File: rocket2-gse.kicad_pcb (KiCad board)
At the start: 4 copper layers, 0 parts

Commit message: Add PCB basic functional blocks
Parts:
- added C1: 4.7uF, Capacitor_SMD:C_0603_1608Metric, F.Cu at (169.0, 137.0)
- added C10: 100nF, Capacitor_SMD:C_0402_1005Metric, F.Cu at (366.1, 71.8)
- added C11: 22uF, Capacitor_SMD:C_1206_3216Metric, F.Cu at (-127.0, 236.0)
- added C12: 100uF, Capacitor_SMD:C_1206_3216Metric, F.Cu at (-143.5, 236.0)
- added C13: 22uF, Capacitor_SMD:C_1206_3216Metric, F.Cu at (-92.5, 236.0)
- added C14: 100uF, Capacitor_SMD:C_1206_3216Metric, F.Cu at (-109.0, 236.0)
- added C15: 4.7uF, Capacitor_SMD:C_0603_1608Metric, F.Cu at (363.8, 78.5)
- added C16: 10uF, Capacitor_SMD:C_1206_3216Metric, F.Cu at (-127.0, 152.5)
- added C17: 10uF, Capacitor_SMD:C_1206_3216Metric, F.Cu at (-114.0, 152.5)
- added C18: 100nF, Capacitor_SMD:C_0402_1005Metric, F.Cu at (-136.0, 13.5)
- added C19: 100nF, Capacitor_SMD:C_0402_1005Metric, F.Cu at (-123.0, 13.6)
- added C2: 100nF, Capacitor_SMD:C_0402_1005Metric, F.Cu at (172.5, 137.0)
- added C20: 100nF, Capacitor_SMD:C_0402_1005Metric, F.Cu at (-110.0, 13.5)
- added C21: 100nF, Capacitor_SMD:C_0402_1005Metric, F.Cu at (-97.0, 13.5)
- added C22: 100nF, Capacitor_SMD:C_0402_1005Metric, F.Cu at (-84.0, 13.5)
- added C23: 100nF, Capacitor_SMD:C_0402_1005Metric, F.Cu at (-71.0, 13.5)
- added C24: 100nF, Capacitor_SMD:C_0402_1005Metric, F.Cu at (-58.0, 13.5)
- added C25: 100nF, Capacitor_SMD:C_0402_1005Metric, F.Cu at (-45.0, 13.5)
- added C26: 100nF, Capacitor_SMD:C_0402_1005Metric, F.Cu at (-32.0, 13.5)
- added C27: 100nF, Capacitor_SMD:C_0402_1005Metric, F.Cu at (-136.5, 62.5)
- added C28: 100nF, Capacitor_SMD:C_0402_1005Metric, F.Cu at (-123.5, 62.5)
- added C29: 100nF, Capacitor_SMD:C_0402_1005Metric, F.Cu at (-110.5, 62.5)
- added C3: 100nF, Capacitor_SMD:C_0402_1005Metric, F.Cu at (176.0, 150.5)
- added C30: 100nF, Capacitor_SMD:C_0402_1005Metric, F.Cu at (-97.5, 62.5)
- added C31: 100nF, Capacitor_SMD:C_0402_1005Metric, F.Cu at (-84.5, 62.5)
- added C32: 100nF, Capacitor_SMD:C_0402_1005Metric, F.Cu at (-137.0, 105.5)
- added C33: 10nF, Capacitor_SMD:C_0402_1005Metric, F.Cu at (-141.0, 108.0)
- added C34: 10nF, Capacitor_SMD:C_0402_1005Metric, F.Cu at (-121.0, 108.0)
- added C35: 100nF, Capacitor_SMD:C_0402_1005Metric, F.Cu at (-117.0, 105.5)
- added C36: 10nF, Capacitor_SMD:C_0402_1005Metric, F.Cu at (-101.0, 108.0)
- added C37: 100nF, Capacitor_SMD:C_0402_1005Metric, F.Cu at (-97.0, 105.5)
- added C38: 10nF, Capacitor_SMD:C_0402_1005Metric, F.Cu at (-81.0, 108.0)
- added C39: 100nF, Capacitor_SMD:C_0402_1005Metric, F.Cu at (-77.0, 105.5)
- added C4: 100nF, Capacitor_SMD:C_0402_1005Metric, F.Cu at (182.5, 150.5)
- added C40: 10nF, Capacitor_SMD:C_0402_1005Metric, F.Cu at (-61.0, 108.0)
- added C41: 100nF, Capacitor_SMD:C_0402_1005Metric, F.Cu at (-57.0, 105.5)
- added C42: 10nF, Capacitor_SMD:C_0402_1005Metric, F.Cu at (-41.0, 108.0)
- added C43: 100nF, Capacitor_SMD:C_0402_1005Metric, F.Cu at (-37.0, 105.5)
- added C44: 100nF, Capacitor_SMD:C_0402_1005Metric, F.Cu at (169.0, 139.0)
- added C5: 100nF, Capacitor_SMD:C_0402_1005Metric, F.Cu at (186.0, 137.0)
- added C6: 100nF, Capacitor_SMD:C_0402_1005Metric, F.Cu at (175.5, 133.5)
- added C7: 1uF, Capacitor_SMD:C_0402_1005Metric, F.Cu at (168.5, 144.0)
- added C8: 100nF, Capacitor_SMD:C_0402_1005Metric, F.Cu at (169.5, 144.0)
- added C9: 10nF, Capacitor_SMD:C_0402_1005Metric, F.Cu at (170.5, 144.0)
- added D1: SDT8A100P5-7, Diode_SMD:D_PowerDI-5, F.Cu at (-139.0, 187.6)
- added D10: SDT8A100P5-7, Diode_SMD:D_PowerDI-5, F.Cu at (-141.0, 26.0)
- added D11: MMSZ4684T1G, Diode_SMD:D_SOD-123, F.Cu at (-142.0, 17.0)
- added D12: SDT8A100P5-7, Diode_SMD:D_PowerDI-5, F.Cu at (-128.0, 26.1)
- added D13: MMSZ4684T1G, Diode_SMD:D_SOD-123, F.Cu at (-129.0, 17.1)
- added D14: SDT8A100P5-7, Diode_SMD:D_PowerDI-5, F.Cu at (-115.0, 26.0)
- added D15: MMSZ4684T1G, Diode_SMD:D_SOD-123, F.Cu at (-116.0, 17.0)
- added D16: SDT8A100P5-7, Diode_SMD:D_PowerDI-5, F.Cu at (-102.0, 26.0)
- added D17: MMSZ4684T1G, Diode_SMD:D_SOD-123, F.Cu at (-103.0, 17.0)
- added D18: SDT8A100P5-7, Diode_SMD:D_PowerDI-5, F.Cu at (-89.0, 26.0)
- added D19: MMSZ4684T1G, Diode_SMD:D_SOD-123, F.Cu at (-90.0, 17.0)
- added D2: SDT8A100P5-7, Diode_SMD:D_PowerDI-5, F.Cu at (-119.0, 187.6)
- added D20: SDT8A100P5-7, Diode_SMD:D_PowerDI-5, F.Cu at (-76.0, 26.0)
- added D21: MMSZ4684T1G, Diode_SMD:D_SOD-123, F.Cu at (-77.0, 17.0)
- added D22: SDT8A100P5-7, Diode_SMD:D_PowerDI-5, F.Cu at (-63.0, 26.0)
- added D23: MMSZ4684T1G, Diode_SMD:D_SOD-123, F.Cu at (-64.0, 17.0)
- added D24: SDT8A100P5-7, Diode_SMD:D_PowerDI-5, F.Cu at (-50.0, 26.0)
- added D25: MMSZ4684T1G, Diode_SMD:D_SOD-123, F.Cu at (-51.0, 17.0)
- added D26: SDT8A100P5-7, Diode_SMD:D_PowerDI-5, F.Cu at (-37.0, 26.0)
- added D27: MMSZ4684T1G, Diode_SMD:D_SOD-123, F.Cu at (-38.0, 17.0)
- added D28: BZV55-B5V1, Diode_SMD:D_MiniMELF, F.Cu at (-140.0, 68.0)
- added D29: BZV55-B5V1, Diode_SMD:D_MiniMELF, F.Cu at (-127.0, 68.0)
- added D3: SDT8A100P5-7, Diode_SMD:D_PowerDI-5, F.Cu at (-129.4, 230.5)
- added D30: BZV55-B5V1, Diode_SMD:D_MiniMELF, F.Cu at (-114.0, 68.0)
- added D31: BZV55-B5V1, Diode_SMD:D_MiniMELF, F.Cu at (-101.0, 68.0)
- added D32: BZV55-B5V1, Diode_SMD:D_MiniMELF, F.Cu at (-88.0, 68.0)
- added D4: SDT8A100P5-7, Diode_SMD:D_PowerDI-5, F.Cu at (-94.9, 230.5)
- added D5: LED, LED_SMD:LED_0603_1608Metric, F.Cu at (-145.0, 188.5)
- added D6: LED, LED_SMD:LED_0603_1608Metric, F.Cu at (-125.0, 188.5)
- added D7: LED, LED_SMD:LED_0603_1608Metric, F.Cu at (338.4, 69.4)
- added D8: LED, LED_SMD:LED_0603_1608Metric, F.Cu at (-150.5, 238.0)
- added D9: LED, LED_SMD:LED_0603_1608Metric, F.Cu at (-116.0, 238.0)
- added F1: ~, Fuse:Fuseholder_Blade_Mini_Keystone_3568, F.Cu at (333.3, 54.0)
- added FB1: BLM18PG471SH1D, Inductor_SMD:L_0603_1608Metric, F.Cu at (-137.0, 109.0)
- added FB10: BLM18PG471SH1D, Inductor_SMD:L_0603_1608Metric, F.Cu at (-65.0, 109.0)
- added FB11: BLM18PG471SH1D, Inductor_SMD:L_0603_1608Metric, F.Cu at (-37.0, 109.0)
- added FB12: BLM18PG471SH1D, Inductor_SMD:L_0603_1608Metric, F.Cu at (-45.0, 109.0)
- added FB2: BLM18PG471SH1D, Inductor_SMD:L_0603_1608Metric, F.Cu at (-145.0, 109.0)
- added FB3: BLM18PG471SH1D, Inductor_SMD:L_0603_1608Metric, F.Cu at (-117.0, 109.0)
- added FB4: BLM18PG471SH1D, Inductor_SMD:L_0603_1608Metric, F.Cu at (-125.0, 109.0)
- added FB5: BLM18PG471SH1D, Inductor_SMD:L_0603_1608Metric, F.Cu at (-97.0, 109.0)
- added FB6: BLM18PG471SH1D, Inductor_SMD:L_0603_1608Metric, F.Cu at (-105.0, 109.0)
- added FB7: BLM18PG471SH1D, Inductor_SMD:L_0603_1608Metric, F.Cu at (-77.0, 109.0)
- added FB8: BLM18PG471SH1D, Inductor_SMD:L_0603_1608Metric, F.Cu at (-85.0, 109.0)
- added FB9: BLM18PG471SH1D, Inductor_SMD:L_0603_1608Metric, F.Cu at (-57.0, 109.0)
- added J1: ARM Cortex Debug, Connector_PinHeader_1.27mm:PinHeader_2x05_P1.27mm_Vertical_SMD, F.Cu at (191.0, 133.0)
- added J10: Solenoid, TerminalBlock:TerminalBlock_bornier-3_P5.08mm, F.Cu at (-128.0, 33.0)
- added J11: Solenoid, TerminalBlock:TerminalBlock_bornier-3_P5.08mm, F.Cu at (-115.0, 32.9)
- added J12: Solenoid, TerminalBlock:TerminalBlock_bornier-3_P5.08mm, F.Cu at (-102.0, 32.9)
- added J13: Solenoid, TerminalBlock:TerminalBlock_bornier-3_P5.08mm, F.Cu at (-89.0, 32.9)
- added J14: Solenoid, TerminalBlock:TerminalBlock_bornier-3_P5.08mm, F.Cu at (-76.0, 32.9)
- added J15: Solenoid, TerminalBlock:TerminalBlock_bornier-3_P5.08mm, F.Cu at (-63.0, 32.9)
- added J16: Solenoid, TerminalBlock:TerminalBlock_bornier-3_P5.08mm, F.Cu at (-50.0, 32.9)
- added J17: Solenoid, TerminalBlock:TerminalBlock_bornier-3_P5.08mm, F.Cu at (-37.0, 32.9)
- added J18: PT, TerminalBlock:TerminalBlock_bornier-3_P5.08mm, F.Cu at (-141.0, 75.9)
- added J19: PT, TerminalBlock:TerminalBlock_bornier-3_P5.08mm, F.Cu at (-128.0, 75.9)
- added J2: PWR0, Connector_BarrelJack:BarrelJack_Horizontal, F.Cu at (-141.0, 194.0)
- added J20: PT, TerminalBlock:TerminalBlock_bornier-3_P5.08mm, F.Cu at (-115.0, 75.9)
- added J21: PT, TerminalBlock:TerminalBlock_bornier-3_P5.08mm, F.Cu at (-102.0, 75.9)
- added J22: PT, TerminalBlock:TerminalBlock_bornier-3_P5.08mm, F.Cu at (-89.0, 75.9)
- added J3: PWR1, Connector_BarrelJack:BarrelJack_Horizontal, F.Cu at (-121.0, 194.0)
- added J4: USB-C, Connector_USB:USB_C_Receptacle_GCT_USB4105-xx-A_16P_TopMnt_Horizontal, F.Cu at (350.1, 32.2)
- added J5: ALARM, TerminalBlock:TerminalBlock_bornier-2_P5.08mm, F.Cu at (345.1, 42.2)
- added J6: ARM, TerminalBlock:TerminalBlock_bornier-2_P5.08mm, F.Cu at (-141.0, 159.9)
- added J7: E-MATCH, TerminalBlock:TerminalBlock_bornier-2_P5.08mm, F.Cu at (-125.0, 159.9)
- added J8: E-MATCH, TerminalBlock:TerminalBlock_bornier-2_P5.08mm, F.Cu at (-112.0, 159.9)
- added J9: Solenoid, TerminalBlock:TerminalBlock_bornier-3_P5.08mm, F.Cu at (-141.0, 32.9)
- added L1: SRR1208-220ML, Inductor_SMD:L_Bourns_SRR1208_12.7x12.7mm, F.Cu at (-141.0, 228.0)
- added L2: SRR1208-220ML, Inductor_SMD:L_Bourns_SRR1208_12.7x12.7mm, F.Cu at (-106.5, 228.0)
- added Q1: DMP3099L, Package_TO_SOT_SMD:SOT-23-3, F.Cu at (-131.5, 235.0)
- added Q10: DMG3402L, Package_TO_SOT_SMD:SOT-23-3, F.Cu at (-109.0, 26.0)
- added Q11: DMG3402L, Package_TO_SOT_SMD:SOT-23-3, F.Cu at (-96.0, 26.0)
- added Q12: DMG3402L, Package_TO_SOT_SMD:SOT-23-3, F.Cu at (-83.0, 26.0)
- added Q13: DMG3402L, Package_TO_SOT_SMD:SOT-23-3, F.Cu at (-70.0, 26.0)
- added Q14: DMG3402L, Package_TO_SOT_SMD:SOT-23-3, F.Cu at (-57.0, 26.0)
- added Q15: DMG3402L, Package_TO_SOT_SMD:SOT-23-3, F.Cu at (-44.0, 26.0)
- added Q16: DMG3402L, Package_TO_SOT_SMD:SOT-23-3, F.Cu at (-31.0, 26.0)
- added Q2: DMP3099L, Package_TO_SOT_SMD:SOT-23-3, F.Cu at (-97.0, 235.0)
- added Q3: DMG3402L, Package_TO_SOT_SMD:SOT-23-3, F.Cu at (359.2, 76.0)
- added Q4: DMG3402L, Package_TO_SOT_SMD:SOT-23-3, F.Cu at (-123.0, 152.5)
- added Q5: DMG3402L, Package_TO_SOT_SMD:SOT-23-3, F.Cu at (-118.5, 151.5)
- added Q6: DMG3402L, Package_TO_SOT_SMD:SOT-23-3, F.Cu at (-110.0, 152.5)
- added Q7: DMG3402L, Package_TO_SOT_SMD:SOT-23-3, F.Cu at (-105.5, 151.5)
- added Q8: DMG3402L, Package_TO_SOT_SMD:SOT-23-3, F.Cu at (-135.0, 26.0)
- added Q9: DMG3402L, Package_TO_SOT_SMD:SOT-23-3, F.Cu at (-122.0, 26.1)
- added R1: 10K, Resistor_SMD:R_0402_1005Metric, F.Cu at (357.4, 27.9)
- added R10: 3.3K, Resistor_SMD:R_0402_1005Metric, F.Cu at (-142.5, 188.5)
- added R11: 3.3K, Resistor_SMD:R_0402_1005Metric, F.Cu at (-122.5, 188.5)
- added R12: 3.3K, Resistor_SMD:R_0402_1005Metric, F.Cu at (363.2, 29.9)
- added R13: 1K, Resistor_SMD:R_0402_1005Metric, F.Cu at (-148.0, 238.0)
- added R14: 470R, Resistor_SMD:R_0402_1005Metric, F.Cu at (-113.5, 238.0)
- added R15: 5.1K, Resistor_SMD:R_0402_1005Metric, F.Cu at (363.2, 35.9)
- added R16: 5.1K, Resistor_SMD:R_0402_1005Metric, F.Cu at (366.1, 27.9)
- added R17: 10K, Resistor_SMD:R_0402_1005Metric, F.Cu at (366.1, 29.9)
- added R18: 100R, Resistor_SMD:R_0402_1005Metric, F.Cu at (366.1, 31.9)
- added R19: 100K, Resistor_SMD:R_0402_1005Metric, F.Cu at (-138.5, 154.0)
- added R2: 100K, Resistor_SMD:R_0402_1005Metric, F.Cu at (-142.5, 190.5)
- added R20: 15K, Resistor_SMD:R_0402_1005Metric, F.Cu at (-138.5, 151.5)
- added R21: 10K, Resistor_SMD:R_0402_1005Metric, F.Cu at (-124.0, 148.5)
- added R22: 100R, Resistor_SMD:R_0402_1005Metric, F.Cu at (-122.0, 149.0)
- added R23: 33K, Resistor_SMD:R_0402_1005Metric, F.Cu at (-120.0, 154.5)
- added R24: 10K, Resistor_SMD:R_0402_1005Metric, F.Cu at (-118.0, 154.5)
- added R25: 10K, Resistor_SMD:R_0402_1005Metric, F.Cu at (-119.0, 148.5)
- added R26: 10K, Resistor_SMD:R_0402_1005Metric, F.Cu at (-111.0, 148.5)
- added R27: 100R, Resistor_SMD:R_0402_1005Metric, F.Cu at (-109.0, 149.0)
- added R28: 33K, Resistor_SMD:R_0402_1005Metric, F.Cu at (-107.0, 154.5)
- added R29: 10K, Resistor_SMD:R_0402_1005Metric, F.Cu at (-105.0, 154.5)
- added R3: 15K, Resistor_SMD:R_0402_1005Metric, F.Cu at (-144.5, 190.5)
- added R30: 10K, Resistor_SMD:R_0402_1005Metric, F.Cu at (-106.0, 148.5)
- added R31: 10K, Resistor_SMD:R_0402_1005Metric, F.Cu at (-134.0, 19.5)
- added R32: 100R, Resistor_SMD:R_0402_1005Metric, F.Cu at (-134.0, 22.5)
- added R33: 1R, Resistor_SMD:R_2512_6332Metric, F.Cu at (-141.0, 21.0)
- added R34: 1K, Resistor_SMD:R_0402_1005Metric, F.Cu at (-136.5, 19.0)
- added R35: 10K, Resistor_SMD:R_0402_1005Metric, F.Cu at (-121.0, 19.6)
- added R36: 100R, Resistor_SMD:R_0402_1005Metric, F.Cu at (-121.0, 22.6)
- added R37: 1R, Resistor_SMD:R_2512_6332Metric, F.Cu at (-128.0, 21.1)
- added R38: 1K, Resistor_SMD:R_0402_1005Metric, F.Cu at (-123.5, 19.1)
- added R39: 10K, Resistor_SMD:R_0402_1005Metric, F.Cu at (-108.0, 19.5)
- added R4: 100K, Resistor_SMD:R_0402_1005Metric, F.Cu at (-122.5, 190.5)
- added R40: 100R, Resistor_SMD:R_0402_1005Metric, F.Cu at (-108.0, 22.5)
- added R41: 1R, Resistor_SMD:R_2512_6332Metric, F.Cu at (-115.0, 21.0)
- added R42: 1K, Resistor_SMD:R_0402_1005Metric, F.Cu at (-110.5, 19.0)
- added R43: 10K, Resistor_SMD:R_0402_1005Metric, F.Cu at (-95.0, 19.5)
- added R44: 100R, Resistor_SMD:R_0402_1005Metric, F.Cu at (-95.0, 22.5)
- added R45: 1R, Resistor_SMD:R_2512_6332Metric, F.Cu at (-102.0, 21.0)
- added R46: 1K, Resistor_SMD:R_0402_1005Metric, F.Cu at (-97.5, 19.0)
- added R47: 10K, Resistor_SMD:R_0402_1005Metric, F.Cu at (-82.0, 19.5)
- added R48: 100R, Resistor_SMD:R_0402_1005Metric, F.Cu at (-82.0, 22.5)
- added R49: 1R, Resistor_SMD:R_2512_6332Metric, F.Cu at (-89.0, 21.0)
- added R5: 15K, Resistor_SMD:R_0402_1005Metric, F.Cu at (-124.5, 190.5)
- added R50: 1K, Resistor_SMD:R_0402_1005Metric, F.Cu at (-84.5, 19.0)
- added R51: 10K, Resistor_SMD:R_0402_1005Metric, F.Cu at (-69.0, 19.5)
- added R52: 100R, Resistor_SMD:R_0402_1005Metric, F.Cu at (-69.0, 22.5)
- added R53: 1R, Resistor_SMD:R_2512_6332Metric, F.Cu at (-76.0, 21.0)
- added R54: 1K, Resistor_SMD:R_0402_1005Metric, F.Cu at (-71.5, 19.0)
- added R55: 10K, Resistor_SMD:R_0402_1005Metric, F.Cu at (-56.0, 19.5)
- added R56: 100R, Resistor_SMD:R_0402_1005Metric, F.Cu at (-56.0, 22.5)
- added R57: 1R, Resistor_SMD:R_2512_6332Metric, F.Cu at (-63.0, 21.0)
- added R58: 1K, Resistor_SMD:R_0402_1005Metric, F.Cu at (-58.5, 19.0)
- added R59: 10K, Resistor_SMD:R_0402_1005Metric, F.Cu at (-43.0, 19.5)
- added R6: 100K, Resistor_SMD:R_0402_1005Metric, F.Cu at (-144.0, 238.0)
- added R60: 100R, Resistor_SMD:R_0402_1005Metric, F.Cu at (-43.0, 22.5)
- added R61: 1R, Resistor_SMD:R_2512_6332Metric, F.Cu at (-50.0, 21.0)
- added R62: 1K, Resistor_SMD:R_0402_1005Metric, F.Cu at (-45.5, 19.0)
- added R63: 10K, Resistor_SMD:R_0402_1005Metric, F.Cu at (-30.0, 19.5)
- added R64: 100R, Resistor_SMD:R_0402_1005Metric, F.Cu at (-30.0, 22.5)
- added R65: 1R, Resistor_SMD:R_2512_6332Metric, F.Cu at (-37.0, 21.0)
- added R66: 1K, Resistor_SMD:R_0402_1005Metric, F.Cu at (-32.5, 19.0)
- added R67: 1K, Resistor_SMD:R_0402_1005Metric, F.Cu at (-138.0, 70.5)
- added R68: 5K, Resistor_SMD:R_0402_1005Metric, F.Cu at (-135.5, 68.0)
- added R69: 10K, Resistor_SMD:R_0402_1005Metric, F.Cu at (-135.5, 70.5)
- added R7: 33K, Resistor_SMD:R_0402_1005Metric, F.Cu at (-142.0, 238.0)
- added R70: 1K, Resistor_SMD:R_0402_1005Metric, F.Cu at (-125.0, 70.5)
- added R71: 5K, Resistor_SMD:R_0402_1005Metric, F.Cu at (-122.5, 68.0)
- added R72: 10K, Resistor_SMD:R_0402_1005Metric, F.Cu at (-122.5, 70.5)
- added R73: 1K, Resistor_SMD:R_0402_1005Metric, F.Cu at (-112.0, 70.5)
- added R74: 5K, Resistor_SMD:R_0402_1005Metric, F.Cu at (-109.5, 68.0)
- added R75: 10K, Resistor_SMD:R_0402_1005Metric, F.Cu at (-109.5, 70.5)
- added R76: 1K, Resistor_SMD:R_0402_1005Metric, F.Cu at (-99.0, 70.5)
- added R77: 5K, Resistor_SMD:R_0402_1005Metric, F.Cu at (-96.5, 68.0)
- added R78: 10K, Resistor_SMD:R_0402_1005Metric, F.Cu at (-96.5, 70.5)
- added R79: 1K, Resistor_SMD:R_0402_1005Metric, F.Cu at (-86.0, 70.5)
- added R8: 33K, Resistor_SMD:R_0402_1005Metric, F.Cu at (-109.5, 238.0)
- added R80: 5K, Resistor_SMD:R_0402_1005Metric, F.Cu at (-83.5, 68.0)
- added R81: 10K, Resistor_SMD:R_0402_1005Metric, F.Cu at (-83.5, 70.5)
- added R9: 20K, Resistor_SMD:R_0402_1005Metric, F.Cu at (-107.5, 238.0)
- added TC1: Thermocouple, UCIRP-KiCAD-Lib:AM-K-PCB, F.Cu at (-141.0, 125.0)
- added TC2: Thermocouple, UCIRP-KiCAD-Lib:AM-K-PCB, F.Cu at (-121.0, 125.0)
- added TC3: Thermocouple, UCIRP-KiCAD-Lib:AM-K-PCB, F.Cu at (-101.0, 125.0)
- added TC4: Thermocouple, UCIRP-KiCAD-Lib:AM-K-PCB, F.Cu at (-81.0, 125.0)
- added TC5: Thermocouple, UCIRP-KiCAD-Lib:AM-K-PCB, F.Cu at (-61.0, 125.0)
- added TC6: Thermocouple, UCIRP-KiCAD-Lib:AM-K-PCB, F.Cu at (-41.0, 125.0)
- added TP1: +24V, TestPoint:TestPoint_Pad_D4.0mm, F.Cu at (353.6, 58.8)
- added TP2: +5V, TestPoint:TestPoint_Pad_D4.0mm, F.Cu at (353.6, 64.9)
- added TP3: +3.3V, TestPoint:TestPoint_Pad_D4.0mm, F.Cu at (353.6, 70.9)
- added TP4: GND, TestPoint:TestPoint_Pad_D4.0mm, F.Cu at (353.6, 77.0)
- added U1: ~, Package_QFP:LQFP-64_10x10mm_P0.5mm, F.Cu at (179.0, 142.0)
- added U10: ~, Package_TO_SOT_SMD:SOT-23-5, F.Cu at (-72.0, 16.0)
- added U11: ~, Package_TO_SOT_SMD:SOT-23-5, F.Cu at (-59.0, 16.0)
- added U12: ~, Package_TO_SOT_SMD:SOT-23-5, F.Cu at (-46.0, 16.0)
- added U13: ~, Package_TO_SOT_SMD:SOT-23-5, F.Cu at (-33.0, 16.0)
- added U14: ~, Package_TO_SOT_SMD:SOT-23-5, F.Cu at (-137.0, 65.0)
- added U15: ~, Package_TO_SOT_SMD:SOT-23-5, F.Cu at (-124.0, 65.0)
- added U16: ~, Package_TO_SOT_SMD:SOT-23-5, F.Cu at (-111.0, 65.0)
- added U17: ~, Package_TO_SOT_SMD:SOT-23-5, F.Cu at (-98.0, 65.0)
- added U18: ~, Package_TO_SOT_SMD:SOT-23-5, F.Cu at (-85.0, 65.0)
- added U19: ~, Package_SO:SOIC-8_3.9x4.9mm_P1.27mm, F.Cu at (-141.0, 103.0)
- added U2: ~, Package_SO:VSSOP-8_3.0x3.0mm_P0.65mm, F.Cu at (-137.0, 236.5)
- added U20: ~, Package_SO:SOIC-8_3.9x4.9mm_P1.27mm, F.Cu at (-121.0, 103.0)
- added U21: ~, Package_SO:SOIC-8_3.9x4.9mm_P1.27mm, F.Cu at (-101.0, 103.0)
- added U22: ~, Package_SO:SOIC-8_3.9x4.9mm_P1.27mm, F.Cu at (-81.0, 103.0)
- added U23: ~, Package_SO:SOIC-8_3.9x4.9mm_P1.27mm, F.Cu at (-61.0, 103.0)
- added U24: ~, Package_SO:SOIC-8_3.9x4.9mm_P1.27mm, F.Cu at (-41.0, 103.0)
- added U25: ~, Package_TO_SOT_THT:TO-220-3_Vertical, F.Cu at (-138.5, 243.1)
- added U26: ~, Package_TO_SOT_THT:TO-220-3_Vertical, F.Cu at (-104.0, 243.1)
- added U3: ~, Package_SO:VSSOP-8_3.0x3.0mm_P0.65mm, F.Cu at (-102.5, 236.5)
- added U4: ~, UCIRP-KiCAD-Lib:GC-XPORT, F.Cu at (326.8, 28.2)
- added U5: ~, Package_TO_SOT_SMD:SOT-23-5, F.Cu at (-137.0, 16.0)
- added U6: ~, Package_TO_SOT_SMD:SOT-23-5, F.Cu at (-124.0, 16.1)
- added U7: ~, Package_TO_SOT_SMD:SOT-23-5, F.Cu at (-111.0, 16.0)
- added U8: ~, Package_TO_SOT_SMD:SOT-23-5, F.Cu at (-98.0, 16.0)
- added U9: ~, Package_TO_SOT_SMD:SOT-23-5, F.Cu at (-85.0, 16.0)
- added Y1: 16MHz, Crystal:Crystal_SMD_2016-4Pin_2.0x1.6mm, F.Cu at (169.0, 141.0)
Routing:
- net +3.3V: track 0.00 -> 37.0 mm, vias 0 -> 29
- net /E-Match0/PWR: track 0.00 -> 25.2 mm
- net Net-(J8-Pin_2): track 0.00 -> 15.2 mm
- net Net-(J7-Pin_2): track 0.00 -> 15.2 mm
- net +5V: track 0.00 -> 11.7 mm, vias 0 -> 17
- net Net-(J22-Pin_2): track 0.00 -> 11.2 mm
- net Net-(J21-Pin_2): track 0.00 -> 11.2 mm
- net Net-(J20-Pin_2): track 0.00 -> 11.2 mm
- net Net-(J19-Pin_2): track 0.00 -> 11.2 mm
- net Net-(J18-Pin_2): track 0.00 -> 11.2 mm
- net SOLENOID1_EN: track 0.00 -> 10.6 mm
- net SOLENOID7_EN: track 0.00 -> 10.6 mm
- net SOLENOID6_EN: track 0.00 -> 10.6 mm
- net SOLENOID4_EN: track 0.00 -> 10.6 mm
- net SOLENOID5_EN: track 0.00 -> 10.6 mm
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- added copper zone on F.Cu, net +24V
- added copper zone on F.Cu, net +3.3V
- added copper zone on F.Cu, net +5V
- added copper zone on F.Cu, net GND
- added copper zone on F.Cu, net Net-(D10-A)
- added copper zone on F.Cu, net Net-(D12-A)
- added copper zone on F.Cu, net Net-(D14-A)
- added copper zone on F.Cu, net Net-(D16-A)
- added copper zone on F.Cu, net Net-(D18-A)
- added copper zone on F.Cu, net Net-(D20-A)
- added copper zone on F.Cu, net Net-(D22-A)
- added copper zone on F.Cu, net Net-(D24-A)
- added copper zone on F.Cu, net Net-(D26-A)
- added copper zone on F.Cu, net Net-(D3-K)
- added copper zone on F.Cu, net Net-(D4-K)
- added copper zone on F.Cu, net Net-(Q10-S)
- added copper zone on F.Cu, net Net-(Q11-S)
- added copper zone on F.Cu, net Net-(Q12-S)
- added copper zone on F.Cu, net Net-(Q13-S)
- added copper zone on F.Cu, net Net-(Q14-S)
- added copper zone on F.Cu, net Net-(Q15-S)
- added copper zone on F.Cu, net Net-(Q16-S)
- added copper zone on F.Cu, net Net-(Q8-S)
- added copper zone on F.Cu, net Net-(Q9-S)
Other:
- board outline added: 3.2 x 15.6 mm
- board text added: "24V"
- board text added: "ARM"
- board text added: "C"
- board text added: "E-MATCH0"
- board text added: "E-MATCH1"
- board text added: "GND"
- board text added: "PT0"
- board text added: "PT1"
- board text added: "PT2"
- board text added: "PT3"
- board text added: "PT4"
- board text added: "S"
- board text added: "S0"
- board text added: "S1"
- board text added: "S2"
- board text added: "S3"
- board text added: "S4"
- board text added: "S5"
- board text added: "S6"
- board text added: "S7"
- board text added: "S8"
- board text added: "TC0"
- board text added: "TC1"
- board text added: "TC2"
- board text added: "TC3"
- board text added: "TC4"
- board text added: "TC5"

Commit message: Full PCB
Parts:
- added REF**: UCIRP_Logo_2, UCIRP-KiCAD-Lib:UCIRP_Logo_2, F.Cu at (126.0, 124.0)
- moved D5 383.4 mm to (238.0, 172.0), turned to 180 degrees
- moved J2 368.1 mm to (226.0, 166.0), turned to 180 degrees
- moved R3 367.6 mm to (222.5, 169.5), turned to 90 degrees
- moved R2 365.7 mm to (222.5, 167.5), turned to 90 degrees
- moved D6 364.8 mm to (238.0, 152.0), turned to 180 degrees
- moved R10 363.9 mm to (221.0, 172.0), turned to 180 degrees
- moved FB2 361.6 mm to (214.0, 66.0), turned to 90 degrees
- moved D1 359.4 mm to (219.6, 164.0), turned to 0 degrees
- moved TC1 358.8 mm to (210.0, 50.5), turned to 90 degrees
- moved C33 353.4 mm to (210.0, 67.0), turned to 0 degrees
- moved U19 352.4 mm to (210.0, 72.0), turned to -90 degrees
- moved J3 350.3 mm to (226.0, 146.0), turned to 180 degrees
- moved R5 349.4 mm to (222.5, 149.5), turned to 90 degrees
- moved R4 347.7 mm to (222.5, 147.5), turned to 90 degrees
- moved FB1 345.7 mm to (206.0, 66.0), turned to -90 degrees
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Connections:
- C10 pad 1: Net-(U1-BOOT0) -> MCU_~{RST}
- R1 pad 1: Net-(U1-BOOT0) -> MCU_~{RST}
- U1 pad 60: Net-(U1-BOOT0) -> GND
- U4 pad 3: ETH_nRST -> ETH_~{RST}
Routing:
- net ALARM: track 0.00 -> 164.8 mm, vias 0 -> 2
- net ARMED: track 1.48 -> 159.6 mm, vias 0 -> 2
- net EMATCH0_CONT: track 1.87 -> 152.4 mm, vias 0 -> 2
- net EMATCH1_CONT: track 1.87 -> 152.2 mm, vias 0 -> 2
- net EMATCH0_FIRE: track 1.49 -> 151.3 mm, vias 0 -> 2
- net EMATCH1_FIRE: track 1.49 -> 150.8 mm, vias 0 -> 2
- net PWR0: track 0.00 -> 137.7 mm, vias 0 -> 2
- net TC_SCK: track 0.00 -> 129.9 mm, vias 0 -> 2
- net TC_MISO: track 0.00 -> 128.8 mm
- net PWR1: track 0.00 -> 117.1 mm, vias 0 -> 2
- net USB_VBUS: track 0.00 -> 113.1 mm
- net USB_D+: track 0.00 -> 110.0 mm, vias 0 -> 2
- net USB_D-: track 0.00 -> 109.9 mm, vias 0 -> 2
- net SOLENOID8_EN: track 10.6 -> 119.6 mm
- net PT4: track 2.59 -> 104.0 mm, vias 0 -> 2
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- added copper zone on In2.Cu, net +24V
- added copper zone on In2.Cu, net +3.3V
- added copper zone on In2.Cu, net +5V
- added copper zone on In2.Cu, net /E-Match0/PWR
- added copper zone on B.Cu, net GND
- added copper zone on In1.Cu, net GND
- added copper zone on F.Cu, net Net-(D1-A)
- added copper zone on F.Cu, net Net-(D1-K)
- added copper zone on F.Cu, net Net-(D2-A)
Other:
- board size 3.2 x 15.6 mm -> 180 x 160 mm
- board text added: "+24V"
- board text added: "+3.3V"
- board text added: "+5V"
- board text added: "ALARM"
- board text added: "PWR1"
- board text added: "PWR2"
- board text added: "UCI Rocket Project - Avionics Ground Support Electronics v1.0 03/2024"

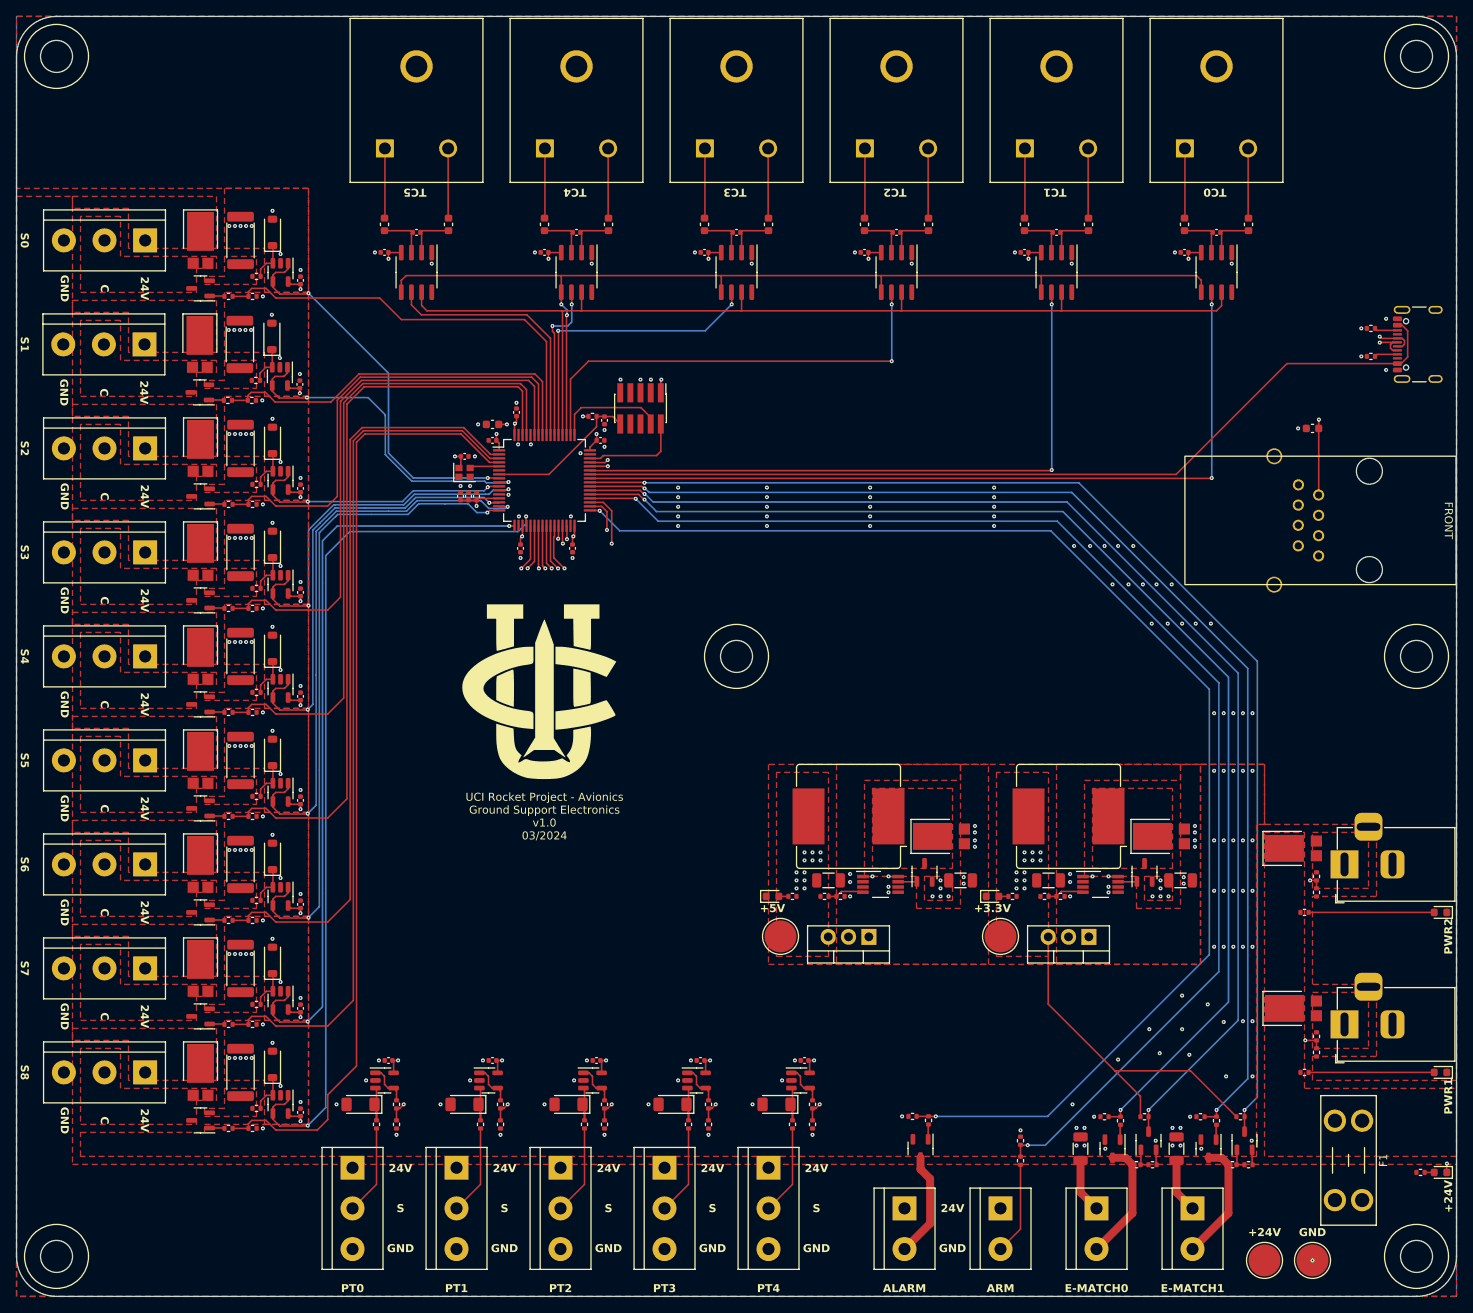
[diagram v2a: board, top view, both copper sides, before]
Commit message: Revise mounting holes, remove test points
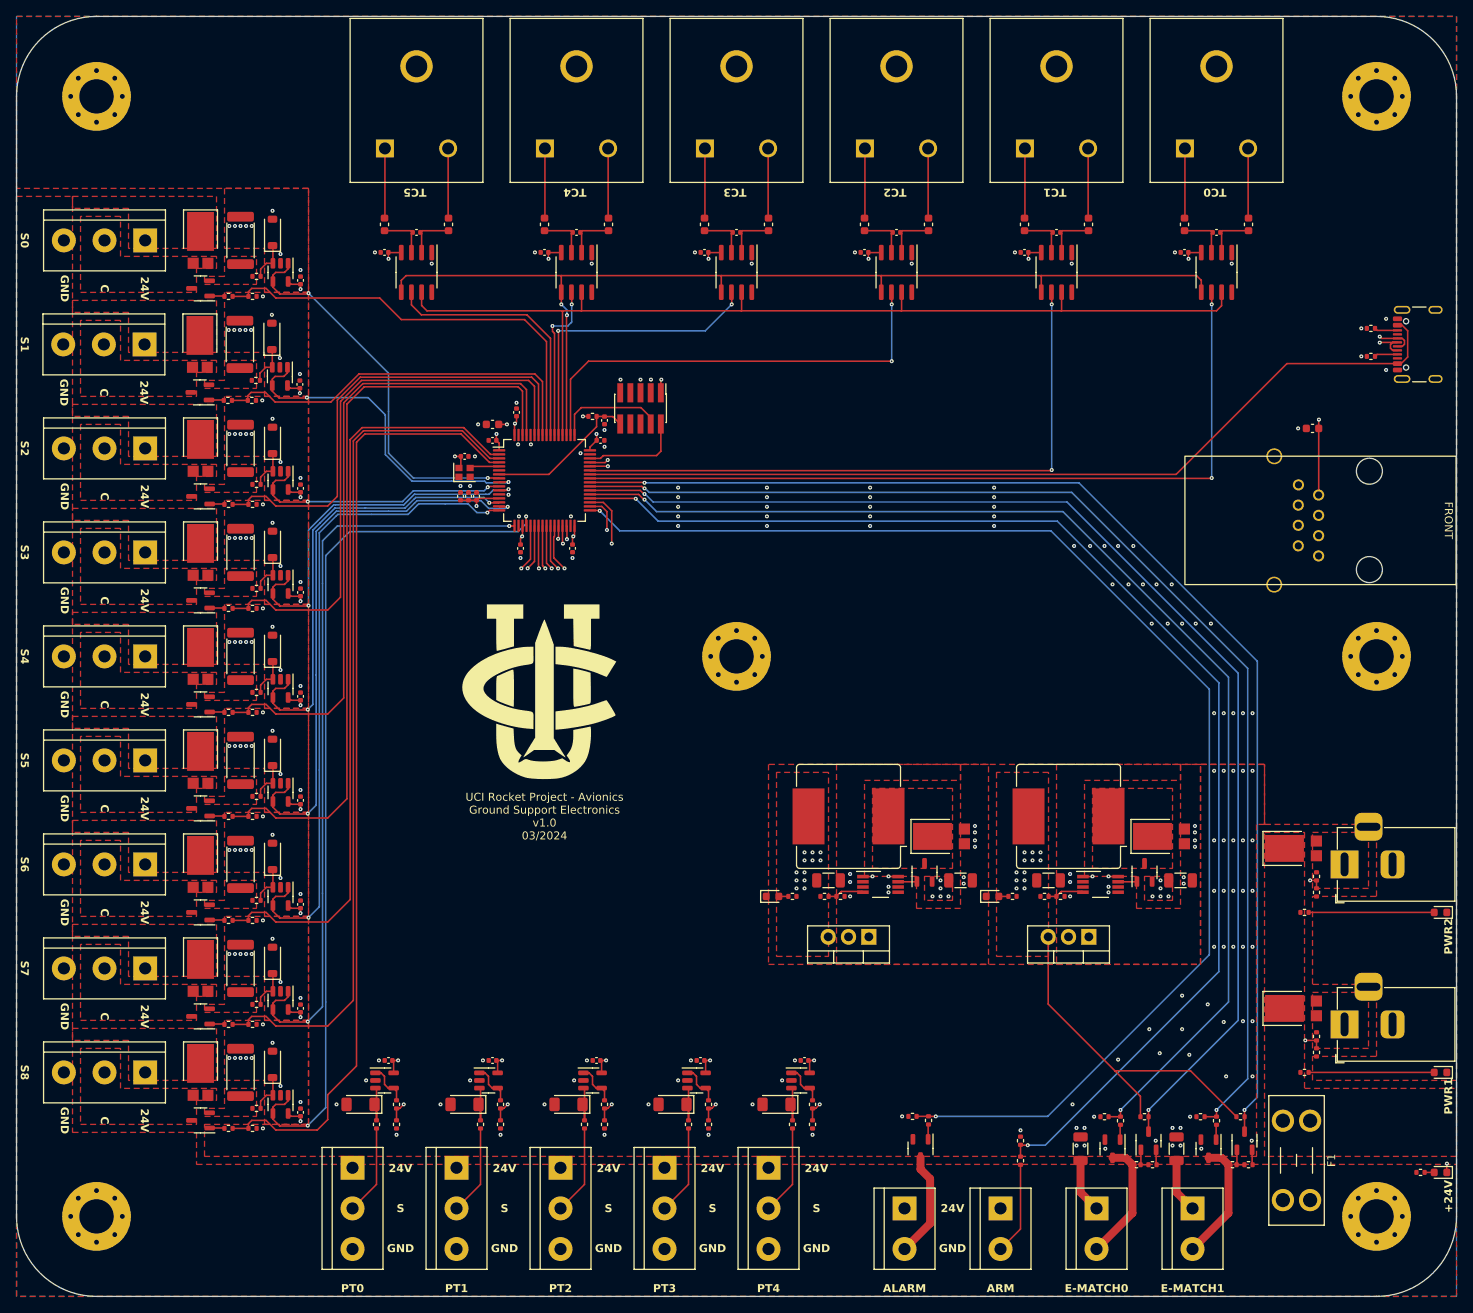
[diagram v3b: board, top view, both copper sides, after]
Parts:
- removed TP1: +24V, TestPoint:TestPoint_Pad_D4.0mm
- removed TP2: +5V, TestPoint:TestPoint_Pad_D4.0mm
- removed TP3: +3.3V, TestPoint:TestPoint_Pad_D4.0mm
- removed TP4: GND, TestPoint:TestPoint_Pad_D4.0mm
- added REF**: MountingHole_4.3mm_M4_Pad_Via, MountingHole:MountingHole_4.3mm_M4_Pad_Via, F.Cu at (150.0, 120.0)
- added REF**: MountingHole_4.3mm_M4_Pad_Via, MountingHole:MountingHole_4.3mm_M4_Pad_Via, F.Cu at (230.0, 190.0)
- added REF**: MountingHole_4.3mm_M4_Pad_Via, MountingHole:MountingHole_4.3mm_M4_Pad_Via, F.Cu at (70.0, 50.0)
- added REF**: MountingHole_4.3mm_M4_Pad_Via, MountingHole:MountingHole_4.3mm_M4_Pad_Via, F.Cu at (70.0, 190.0)
- added REF**: MountingHole_4.3mm_M4_Pad_Via, MountingHole:MountingHole_4.3mm_M4_Pad_Via, F.Cu at (230.0, 50.0)
- added REF**: MountingHole_4.3mm_M4_Pad_Via, MountingHole:MountingHole_4.3mm_M4_Pad_Via, F.Cu at (230.0, 120.0)
- moved F1 6.50 mm to (221.7, 178.0)
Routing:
- net GND: vias 249 -> 248
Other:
- outline, holes or cut-outs redrawn
- board text removed: "+3.3V"
- board text removed: "+5V"

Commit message: Revise USB circuitry
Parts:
- added R82: 33K, Resistor_SMD:R_0402_1005Metric, F.Cu at (225.5, 84.0)
- added R83: 82K, Resistor_SMD:R_0402_1005Metric, F.Cu at (225.5, 86.0)
- added U27: USBLC6-2SC6, Package_TO_SOT_SMD:SOT-23-6, F.Cu at (225.5, 80.5)
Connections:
- J4 pad A4: USB_VBUS -> VBUS
- J4 pad A6: USB_D+ -> Net-(J4-D+-PadA6)
- J4 pad A7: USB_D- -> Net-(J4-D--PadA7)
- J4 pad A9: USB_VBUS -> VBUS
- J4 pad B4: USB_VBUS -> VBUS
- J4 pad B6: USB_D+ -> Net-(J4-D+-PadA6)
- J4 pad B7: USB_D- -> Net-(J4-D--PadA7)
- J4 pad B9: USB_VBUS -> VBUS
- U1 pad 42: USB_VBUS -> Net-(U1-PA9)
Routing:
- net USB_VBUS: track 113.1 -> 0.00 mm
- net Net-(U1-PA9): track 0.00 -> 100.1 mm
- net VBUS: track 0.00 -> 17.5 mm
- net USB_D+: track 110.0 -> 99.4 mm
- net USB_D-: track 109.9 -> 99.5 mm
- net Net-(J4-D+-PadA6): track 0.00 -> 8.71 mm
- net Net-(J4-D--PadA7): track 0.00 -> 7.56 mm
- net GND: vias 248 -> 250
